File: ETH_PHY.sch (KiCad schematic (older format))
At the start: 37 parts, among them J4 BELFUSE_0826-1X1T-HS-F, U4 88E1512-XX-NNP2I000, U6 TXS0102DCUR

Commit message: DDR terminations changed, HTML BoM with variant added
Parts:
- C43, OSC1: config (none) -> dnf
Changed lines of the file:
@@
-EESchema Schematic File Version 5
+EESchema Schematic File Version 4
 LIBS:AMC_FMC_Carrier-PcbDoc-cache
 EELAYER 29 0
@@
 F 3 "" H 4600 3400 50  0001 C CNN
 F 4 "ECS-2520MV-250-BN-TR" H 4600 3400 50  0001 C CNN "PN"
+F 5 "dnf" H 4900 2950 50  0000 C CNN "config"
 	1    4600 3400
 	1    0    0    -1
@@
 F 39 "Capacitors SMD" H 4050 -130 60  0001 L CNN "Library Name"
 F 40 "This work is licensed under the Creative Commons CC-BY-SA 4.0 License. To the extent that circuit schematics that use Licensed Material can be considered to be ‘Adapted Material’, then the copyright holder waives article 3.b of the license with respect to these schematics." H 4050 -220 60  0001 L CNN "License"
+F 41 "dnf" V 4350 3750 50  0000 C CNN "config"
 	1    4050 3550
 	0    1    1    0

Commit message: SW2 placement changed, BOM cleared, FPGA boot, less ERC errors and wornings
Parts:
- removed L3, L4: IND0603_MURATA_BLM18PG121SN1D, INDC1608X95N, symbol Inductors_SMD:IND0603_MURATA_BLM18PG121SN1D
- added L3, L4: IND0603_MURATA_BLM18SG121TN1D, INDC1608X65N, symbol Inductors_SMD:IND0603_MURATA_BLM18SG121TN1D
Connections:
- wire segments 154 -> 155

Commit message: BOM updated, 25MHz clock level fixed
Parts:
- removed R63: R0402_0R_JUMPER, RESC1005X40N, symbol Resistors_SMD:R0402_0R_JUMPER
- added C374, C375: CC0402_100PF_50V_5%_C0G, CAPC1005X55N, symbol Capacitors_SMD:CC0402_100PF_50V_5%_C0G
- OSC1: symbol AMC_FMC_Carrier-PcbDoc-rescue:Oscillator-powerMG -> AMC_FMC_Carrier-PcbDoc-rescue:Oscillator-powerMG-AMC_FMC_Carrier-PcbDoc-rescue
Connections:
- wire segments 155 -> 157

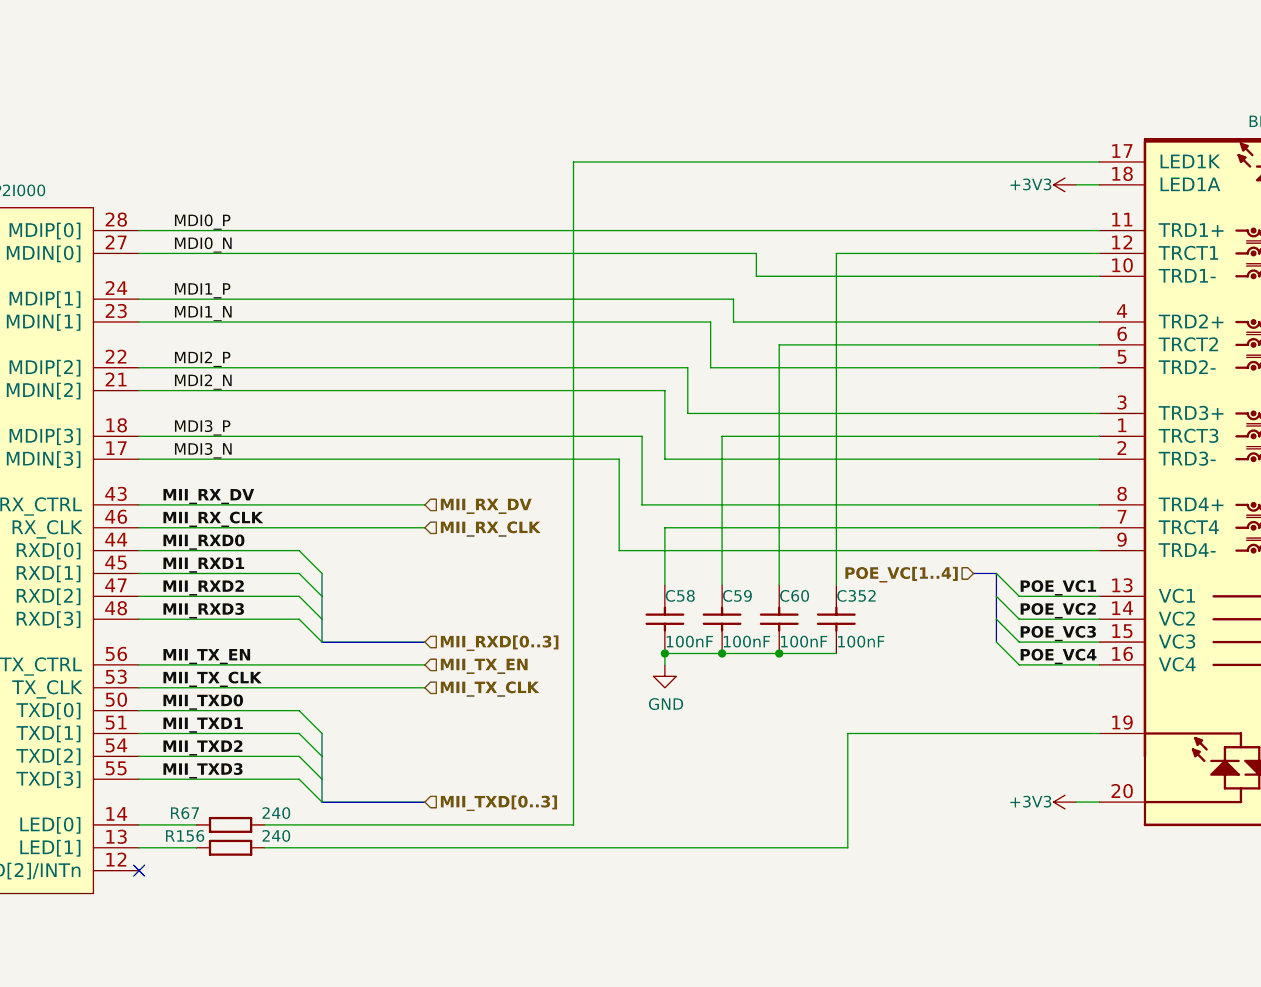
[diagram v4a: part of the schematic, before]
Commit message: U.FL for clock, logos moved, MII -> RGMII, new symbol library, git tag added
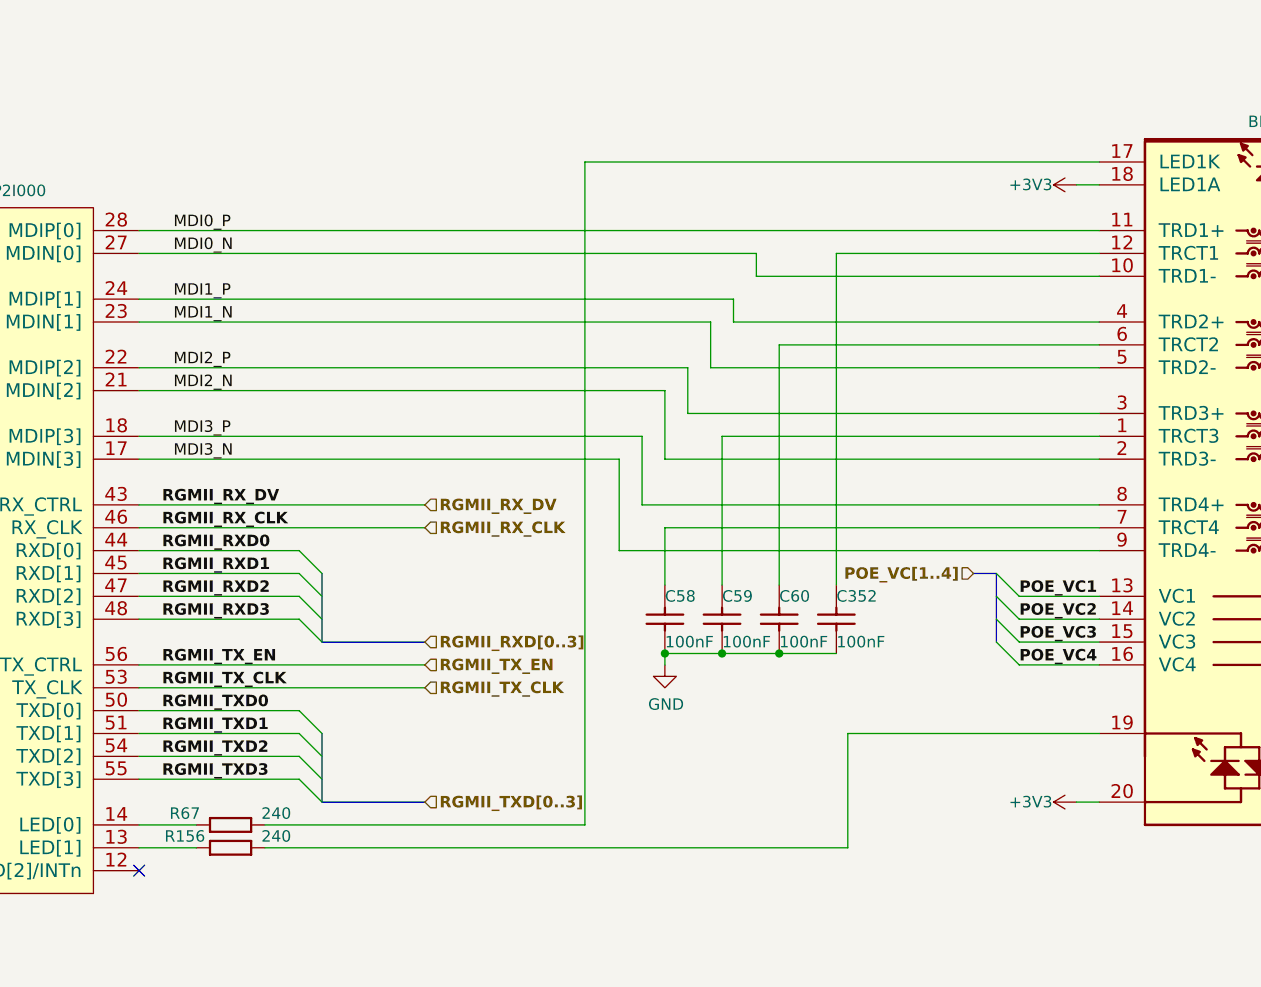
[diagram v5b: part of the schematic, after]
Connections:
- net MII_RXD0 renamed RGMII_RXD0
- net MII_RXD1 renamed RGMII_RXD1
- net MII_RXD2 renamed RGMII_RXD2
- net MII_RXD3 renamed RGMII_RXD3
- net MII_RX_CLK renamed RGMII_RX_CLK
- net MII_RX_DV renamed RGMII_RX_DV
- net MII_TXD0 renamed RGMII_TXD0
- net MII_TXD1 renamed RGMII_TXD1
- net MII_TXD2 renamed RGMII_TXD2
- net MII_TXD3 renamed RGMII_TXD3
- net MII_TX_CLK renamed RGMII_TX_CLK
- net MII_TX_EN renamed RGMII_TX_EN
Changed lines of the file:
@@
 $EndComp
 Text Label 8200 4400 0    50   ~ 10
-MII_TXD0
+RGMII_TXD0
 Text Label 8200 4500 0    50   ~ 10
-MII_TXD1
+RGMII_TXD1
 Text Label 8200 4600 0    50   ~ 10
-MII_TXD2
+RGMII_TXD2
 Text Label 8200 4700 0    50   ~ 10
-MII_TXD3
+RGMII_TXD3
 Text Label 8200 4200 0    50   ~ 10
-MII_TX_EN
+RGMII_TX_EN
 Text Label 8200 4300 0    50   ~ 10
-MII_TX_CLK
+RGMII_TX_CLK
 Text Label 8200 3700 0    50   ~ 10
-MII_RXD0
+RGMII_RXD0
 Text Label 8200 3800 0    50   ~ 10
-MII_RXD1
+RGMII_RXD1
 Text Label 8200 3900 0    50   ~ 10
-MII_RXD2
+RGMII_RXD2
 Text Label 8200 4000 0    50   ~ 10
-MII_RXD3
+RGMII_RXD3
 Text Label 8200 3500 0    50   ~ 10
-MII_RX_DV
+RGMII_RX_DV
 Text Label 8200 3600 0    50   ~ 10
-MII_RX_CLK
+RGMII_RX_CLK
 Wire Wire Line
 	6350 4700 6500 4700
@@
 	8900 4800 9350 4800
 Text HLabel 9350 4100 2    50   Input ~ 10
-MII_RXD[0..3]
+RGMII_RXD[0..3]
 Text HLabel 9350 4800 2    50   Input ~ 10
-MII_TXD[0..3]
+RGMII_TXD[0..3]
 Text HLabel 9350 4200 2    50   Input ~ 10
-MII_TX_EN
+RGMII_TX_EN
 Text HLabel 9350 4300 2    50   Input ~ 10
-MII_TX_CLK
+RGMII_TX_CLK
 Wire Wire Line
 	8100 4200 9350 4200
@@
 	8100 4300 9350 4300
 Text HLabel 9350 3500 2    50   Input ~ 10
-MII_RX_DV
+RGMII_RX_DV
 Text HLabel 9350 3600 2    50   Input ~ 10
-MII_RX_CLK
+RGMII_RX_CLK
 Wire Wire Line
 	8100 3500 9350 3500
@@
 	12200 4800 12300 4800
 Wire Wire Line
-	8650 4900 10000 4900
-Wire Wire Line
-	10000 4900 10000 2000
-Wire Wire Line
-	10000 2000 12300 2000
+	10050 4900 10050 2000
 Wire Wire Line
 	12300 2400 11150 2400
@@
 Entry Wire Line
 	8800 3700 8900 3800
+Wire Wire Line
+	10050 2000 12300 2000
+Wire Wire Line
+	8650 4900 10050 4900
 Wire Bus Line
 	8900 4500 8900 4800

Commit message: RGMII lines tuned, RGMII RX resistors added, MII->RGMII
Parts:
- added R291, R292, R293, R294, R295, R296: R0402_22R_1%_0.0625W_100PPM, RESC1005X40N, symbol Resistors_SMD:R0402_22R_1%_0.0625W_100PPM
- J4: symbol Miscellaneous:BELFUSE_0826-1X1T-HS-F -> AMC_FMC_Carrier-PcbDoc-rescue:BELFUSE_0826-1X1T-HS-F-Miscellaneous
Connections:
- net RGMII_RXD0: now also R293.2; no longer U4.44 (RXD[0])
- net RGMII_RXD1: now also R294.2; no longer U4.45 (RXD[1])
- net RGMII_RXD2: now also R295.2; no longer U4.47 (RXD[2])
- net RGMII_RXD3: now also R296.2; no longer U4.48 (RXD[3])
- net RGMII_RX_CLK: now also R292.2; no longer U4.46 (RX_CLK)
- net RGMII_RX_DV: now also R291.2; no longer U4.43 (RX_CTRL)
- new net: R291.1, U4.43 (RX_CTRL)
- new net: R293.1, U4.44 (RXD[0])
- new net: R294.1, U4.45 (RXD[1])
- new net: R292.1, U4.46 (RX_CLK)
- new net: R295.1, U4.47 (RXD[2])
- new net: R296.1, U4.48 (RXD[3])
